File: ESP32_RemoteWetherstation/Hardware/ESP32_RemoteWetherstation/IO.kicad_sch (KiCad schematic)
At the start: 0 parts

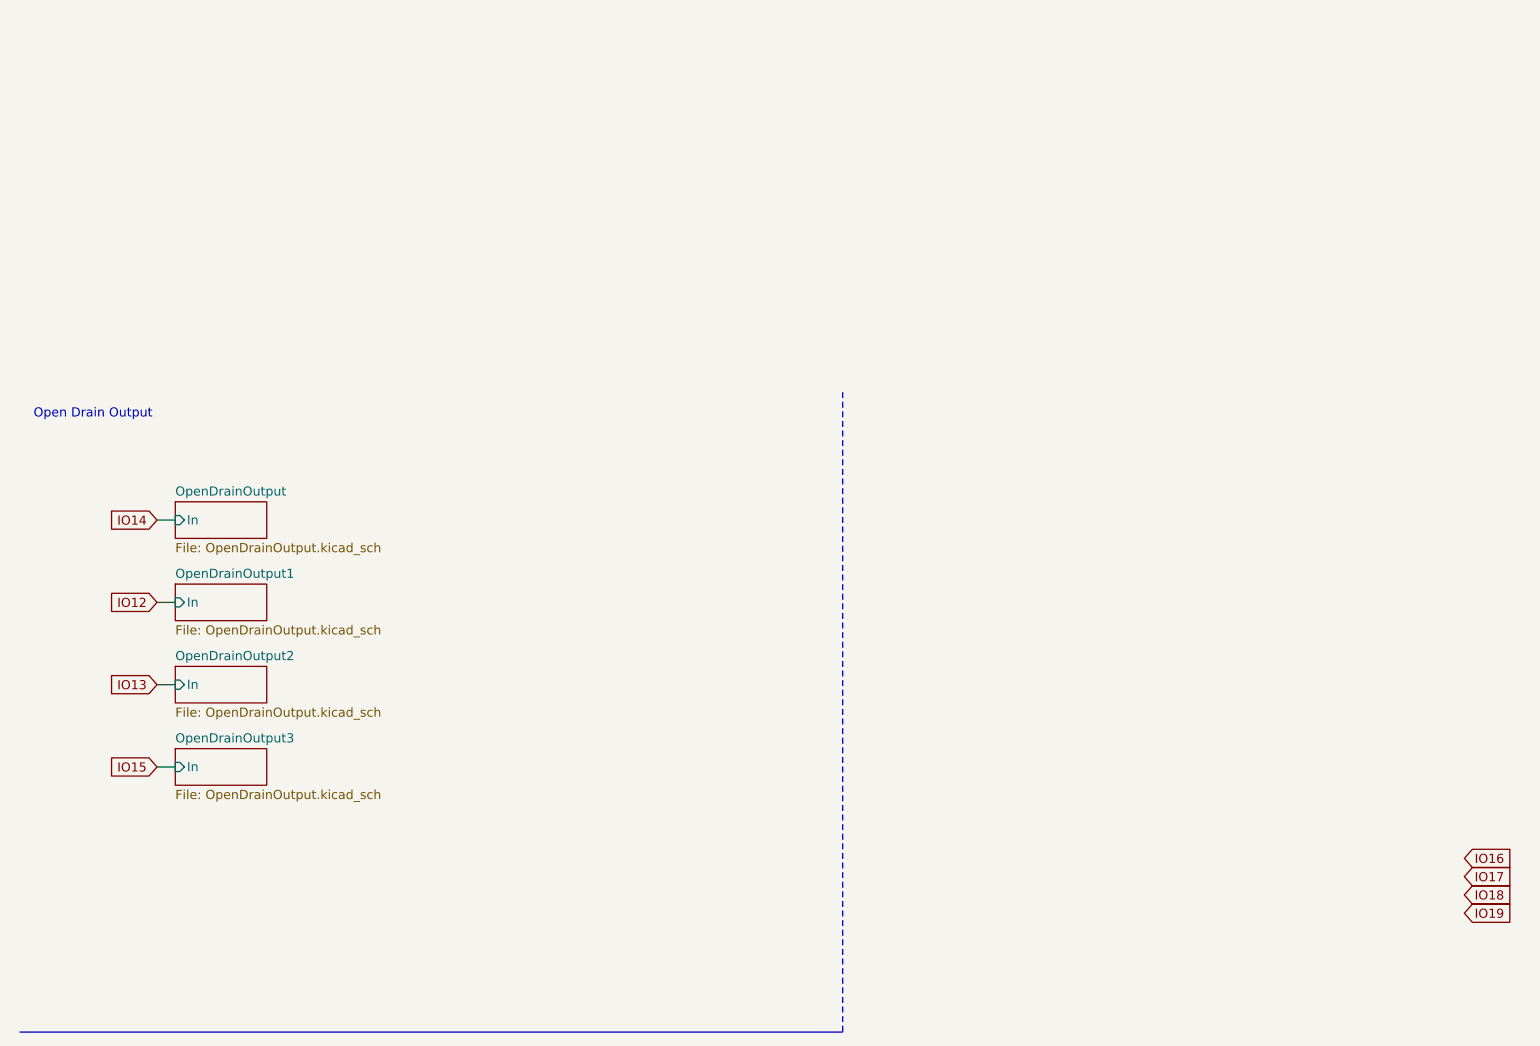
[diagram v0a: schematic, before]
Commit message: added Inputs
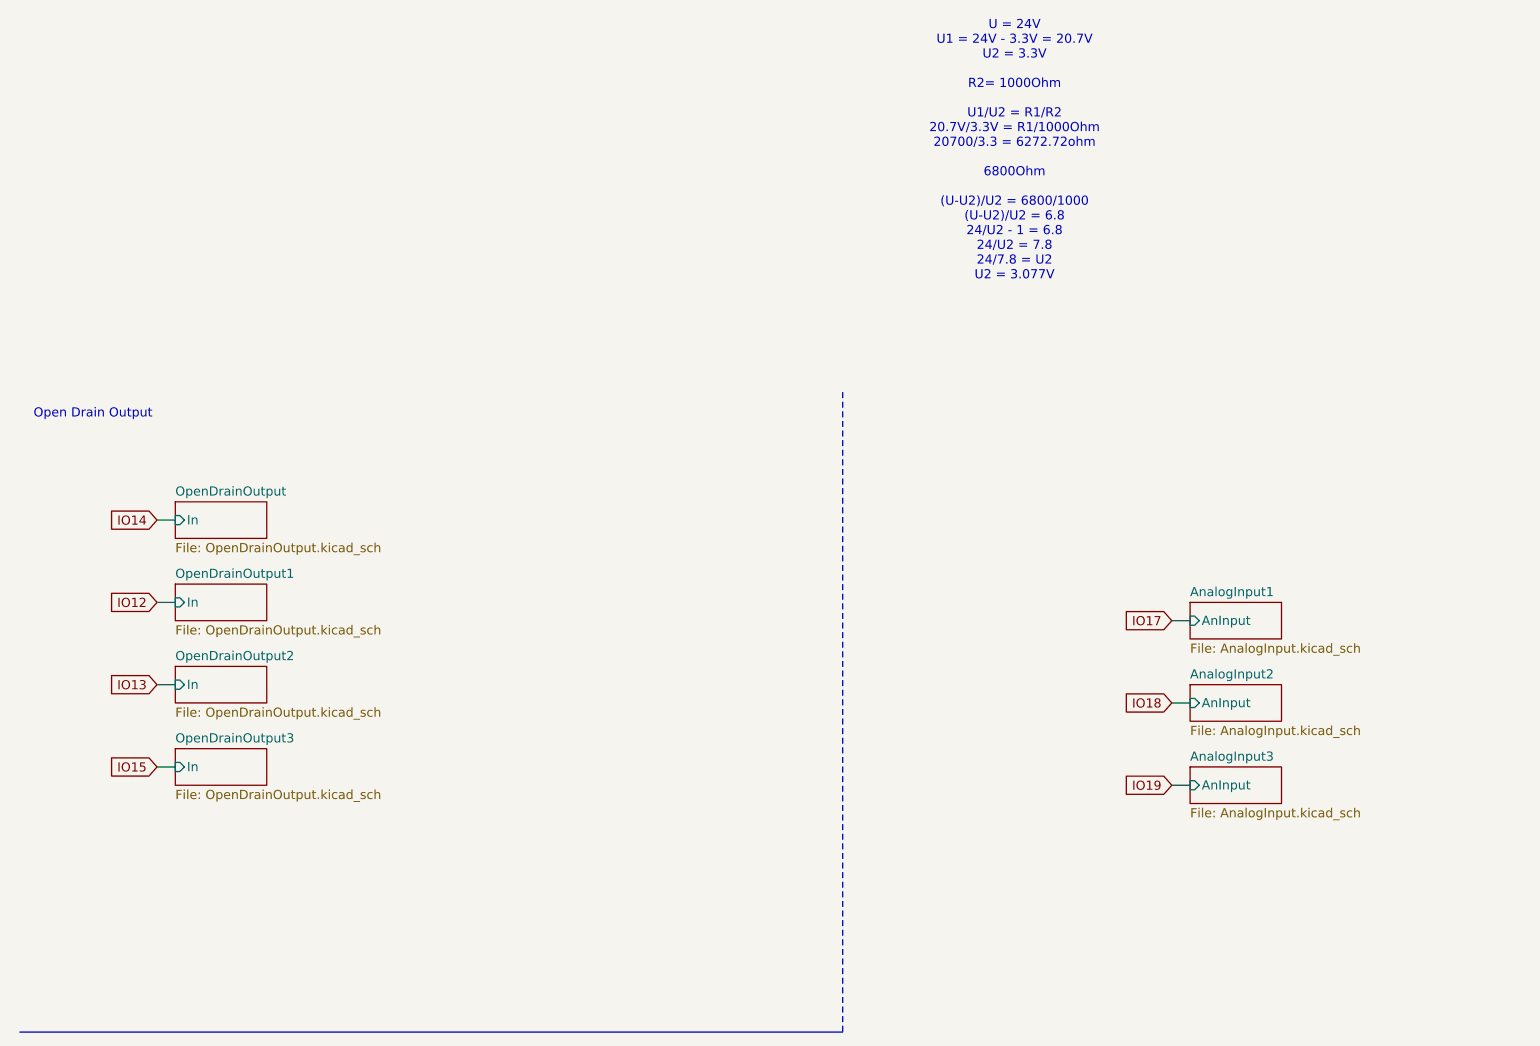
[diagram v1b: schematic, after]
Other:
- added sheet AnalogInput1 (AnalogInput.kicad_sch)
- added sheet AnalogInput2 (AnalogInput.kicad_sch)
- added sheet AnalogInput3 (AnalogInput.kicad_sch)
- note added: "U = 24V U1 = 24V - 3.3V = 20.7V U2 = 3.3V R2= 1000Ohm U1/U2 = R1/R2 20.7V/3.3V = R1/1000Ohm 20700/3.3 = 6272.72ohm 6800Ohm (U-U2)/U2 = 6800/1000 (U-U2)/U2 = 6.8 24/U2 - 1 = 6.8 24/U2 = 7.8 24/7.8 = U2 U2 = 3.077V"
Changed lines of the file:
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@@
+		)
+	)
+	(text "U = 24V\nU1 = 24V - 3.3V = 20.7V\nU2 = 3.3V\n\nR2= 1000Ohm\n\nU1/U2 = R1/R2\n20.7V/3.3V = R1/1000Ohm\n20700/3.3 = 6272.72ohm\n\n6800Ohm\n\n(U-U2)/U2 = 6800/1000\n(U-U2)/U2 = 6.8\n24/U2 - 1 = 6.8\n24/U2 = 7.8\n24/7.8 = U2\nU2 = 3.077V"
+		(exclude_from_sim no)
+		(at 150.876 -20.828 0)
+		(effects
+			(font
+				(size 1.27 1.27)
+			)
 		)
 	)
@@
 	(wire
 		(pts
+			(xy 172.72 67.31) (xy 175.26 67.31)
+		)
+		(stroke
+			(width 0)
+			(type default)
+		)
+	)
+	(wire
+		(pts
 			(xy 31.75 30.48) (xy 34.29 30.48)
 		)
@@
 		)
 	)
+	(wire
+		(pts
+			(xy 172.72 44.45) (xy 175.26 44.45)
+		)
+		(stroke
+			(width 0)
+			(type default)
+		)
+	)
+	(wire
+		(pts
+			(xy 172.72 55.88) (xy 175.26 55.88)
+		)
+		(stroke
+			(width 0)
+			(type default)
+		)
+	)
 	(global_label "IO14"
 		(shape input)
@@
 	(global_label "IO18"
 		(shape input)
-		(at 213.36 82.55 0)
-		(fields_autoplaced yes)
-		(effects
-			(font
-				(size 1.27 1.27)
-			)
-			(justify left)
-		)
-		(property "Intersheetrefs" "${INTERSHEET_REFS}"
-			(at 220.6995 82.55 0)
-			(effects
-				(font
-					(size 1.27 1.27)
-				)
-				(justify left)
+		(at 172.72 55.88 180)
+		(fields_autoplaced yes)
+		(effects
+			(font
+				(size 1.27 1.27)
+			)
+			(justify right)
+		)
+		(property "Intersheetrefs" "${INTERSHEET_REFS}"
+			(at 165.3805 55.88 0)
+			(effects
+				(font
+					(size 1.27 1.27)
+				)
+				(justify right)
 				(hide yes)
 			)
@@
 		)
 	)
-	(global_label "IO16"
-		(shape input)
-		(at 213.36 77.47 0)
-		(fields_autoplaced yes)
-		(effects
-			(font
-				(size 1.27 1.27)
-			)
-			(justify left)
-		)
-		(property "Intersheetrefs" "${INTERSHEET_REFS}"
-			(at 220.6995 77.47 0)
-			(effects
-				(font
-					(size 1.27 1.27)
-				)
-				(justify left)
-				(hide yes)
-			)
-		)
-	)
 	(global_label "IO19"
 		(shape input)
-		(at 213.36 85.09 0)
-		(fields_autoplaced yes)
-		(effects
-			(font
-				(size 1.27 1.27)
-			)
-			(justify left)
-		)
-		(property "Intersheetrefs" "${INTERSHEET_REFS}"
-			(at 220.6995 85.09 0)
-			(effects
-				(font
-					(size 1.27 1.27)
-				)
-				(justify left)
+		(at 172.72 67.31 180)
+		(fields_autoplaced yes)
+		(effects
+			(font
+				(size 1.27 1.27)
+			)
+			(justify right)
+		)
+		(property "Intersheetrefs" "${INTERSHEET_REFS}"
+			(at 165.3805 67.31 0)
+			(effects
+				(font
+					(size 1.27 1.27)
+				)
+				(justify right)
 				(hide yes)
 			)
@@
 	(global_label "IO17"
 		(shape input)
-		(at 213.36 80.01 0)
-		(fields_autoplaced yes)
-		(effects
-			(font
-				(size 1.27 1.27)
-			)
-			(justify left)
-		)
-		(property "Intersheetrefs" "${INTERSHEET_REFS}"
-			(at 220.6995 80.01 0)
-			(effects
-				(font
-					(size 1.27 1.27)
-				)
-				(justify left)
+		(at 172.72 44.45 180)
+		(fields_autoplaced yes)
+		(effects
+			(font
+				(size 1.27 1.27)
+			)
+			(justify right)
+		)
+		(property "Intersheetrefs" "${INTERSHEET_REFS}"
+			(at 165.3805 44.45 0)
+			(effects
+				(font
+					(size 1.27 1.27)
+				)
+				(justify right)
 				(hide yes)
 			)
@@
 	)
 	(sheet
+		(at 175.26 64.77)
+		(size 12.7 5.08)
+		(exclude_from_sim no)
+		(in_bom yes)
+		(on_board yes)
+		(dnp no)
+		(fields_autoplaced yes)
+		(stroke
+			(width 0.1524)
+			(type solid)
+		)
+		(fill
+			(color 0 0 0 0.0000)
+		)
+		(property "Sheetname" "AnalogInput3"
+			(at 175.26 64.0584 0)
+			(effects
+				(font
+					(size 1.27 1.27)
+				)
+				(justify left bottom)
+			)
+		)
+		(property "Sheetfile" "AnalogInput.kicad_sch"
+			(at 175.26 70.4346 0)
+			(effects
+				(font
+					(size 1.27 1.27)
+				)
+				(justify left top)
+			)
+		)
+		(pin "AnInput" input
+			(at 175.26 67.31 180)
+			(effects
+				(font
+					(size 1.27 1.27)
+				)
+				(justify left)
+			)
+		)
+		(instances
+			(project "ESP32_RemoteWetherstation"
+				(path "/bb194ab9-ddae-46dd-ae5d-1e0c862ad374/4641ced3-b603-4979-9d30-21d259fc76b1"
+					(page "11")
+				)
+			)
+		)
+	)
+	(sheet
 		(at 34.29 39.37)
 		(size 12.7 5.08)
@@
 	)
 	(sheet
+		(at 175.26 41.91)
+		(size 12.7 5.08)
+		(exclude_from_sim no)
+		(in_bom yes)
+		(on_board yes)
+		(dnp no)
+		(fields_autoplaced yes)
+		(stroke
+			(width 0.1524)
+			(type solid)
+		)
+		(fill
+			(color 0 0 0 0.0000)
+		)
+		(property "Sheetname" "AnalogInput1"
+			(at 175.26 41.1984 0)
+			(effects
+				(font
+					(size 1.27 1.27)
+				)
+				(justify left bottom)
+			)
+		)
+		(property "Sheetfile" "AnalogInput.kicad_sch"
+			(at 175.26 47.5746 0)
+			(effects
+				(font
+					(size 1.27 1.27)
+				)
+				(justify left top)
+			)
+		)
+		(pin "AnInput" input
+			(at 175.26 44.45 180)
+			(effects
+				(font
+					(size 1.27 1.27)
+				)
+				(justify left)
+			)
+		)
+		(instances
+			(project "ESP32_RemoteWetherstation"
+				(path "/bb194ab9-ddae-46dd-ae5d-1e0c862ad374/4641ced3-b603-4979-9d30-21d259fc76b1"
+					(page "8")
+				)
+			)
+		)
+	)
+	(sheet
 		(at 34.29 27.94)
 		(size 12.7 5.08)
@@
 				)
 			)
+		)
+	)
+	(sheet
+		(at 175.26 53.34)
+		(size 12.7 5.08)
+		(exclude_from_sim no)
+		(in_bom yes)
+		(on_board yes)
+		(dnp no)
+		(fields_autoplaced yes)
+		(stroke
+			(width 0.1524)
+			(type solid)
+		)
+		(fill
+			(color 0 0 0 0.0000)
+		)
+		(property "Sheetname" "AnalogInput2"
+			(at 175.26 52.6284 0)
+			(effects
+				(font
+					(size 1.27 1.27)
+				)
+				(justify left bottom)
+			)
+		)
+		(property "Sheetfile" "AnalogInput.kicad_sch"
+			(at 175.26 59.0046 0)
+			(effects
+				(font
+					(size 1.27 1.27)
+				)
+				(justify left top)
+			)
+		)
+		(pin "AnInput" input
+			(at 175.26 55.88 180)
+			(effects
+				(font
+					(size 1.27 1.27)
+				)
+				(justify left)
+			)
+		)
+		(instances
+			(project "ESP32_RemoteWetherstation"
+				(path "/bb194ab9-ddae-46dd-ae5d-1e0c862ad374/4641ced3-b603-4979-9d30-21d259fc76b1"
+					(page "10")
+				)
+			)

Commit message: edited schematic looks
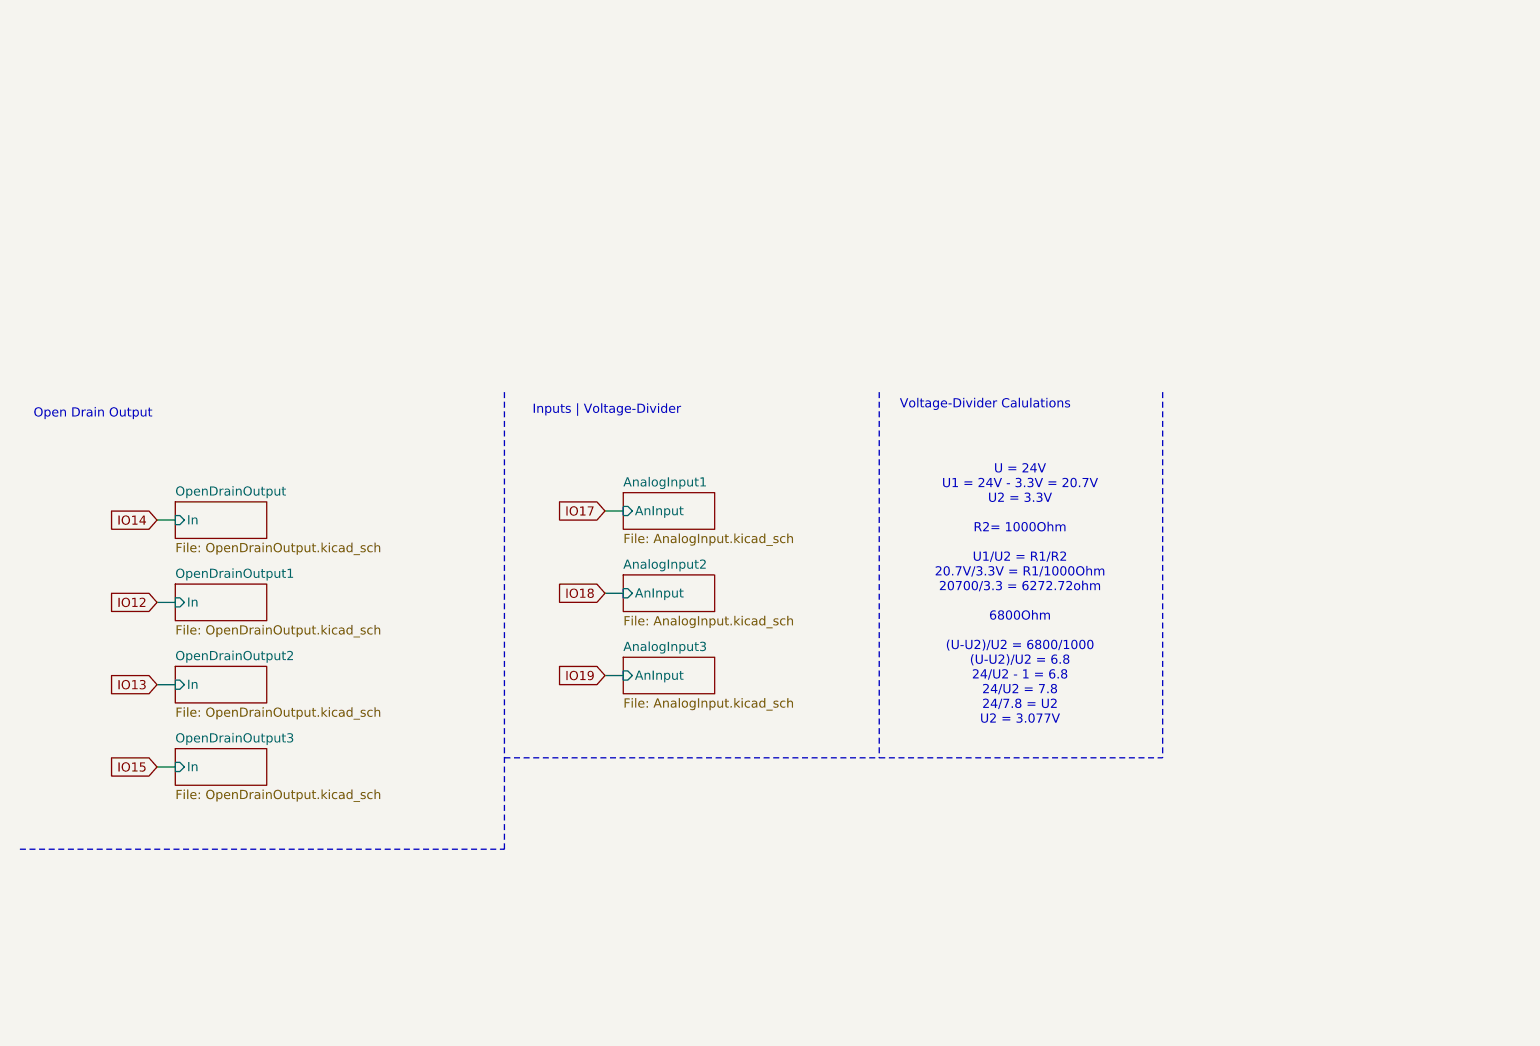
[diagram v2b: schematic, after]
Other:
- note added: "Inputs | Voltage-Divider"
- note added: "Voltage-Divider Calulations"
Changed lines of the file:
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@@
 	(generator_version "9.0")
 	(paper "A4")
+	(text "Voltage-Divider Calulations"
+		(exclude_from_sim no)
+		(at 146.812 14.478 0)
+		(effects
+			(font
+				(size 1.27 1.27)
+			)
+		)
+	)
 	(text "Open Drain Output"
 		(exclude_from_sim no)
@@
 	(text "U = 24V\nU1 = 24V - 3.3V = 20.7V\nU2 = 3.3V\n\nR2= 1000Ohm\n\nU1/U2 = R1/R2\n20.7V/3.3V = R1/1000Ohm\n20700/3.3 = 6272.72ohm\n\n6800Ohm\n\n(U-U2)/U2 = 6800/1000\n(U-U2)/U2 = 6.8\n24/U2 - 1 = 6.8\n24/U2 = 7.8\n24/7.8 = U2\nU2 = 3.077V"
 		(exclude_from_sim no)
-		(at 150.876 -20.828 0)
+		(at 151.638 40.894 0)
+		(effects
+			(font
+				(size 1.27 1.27)
+			)
+		)
+	)
+	(text "Inputs | Voltage-Divider"
+		(exclude_from_sim no)
+		(at 94.234 15.24 0)
 		(effects
 			(font
@@
 	(polyline
 		(pts
-			(xy 12.7 101.6) (xy 127 101.6)
+			(xy 171.45 12.7) (xy 171.45 63.5)
+		)
+		(stroke
+			(width 0)
+			(type dash)
+		)
+	)
+	(wire
+		(pts
+			(xy 93.98 52.07) (xy 96.52 52.07)
 		)
 		(stroke
@@
 	(wire
 		(pts
-			(xy 172.72 67.31) (xy 175.26 67.31)
+			(xy 31.75 30.48) (xy 34.29 30.48)
 		)
 		(stroke
@@
 	(wire
 		(pts
-			(xy 31.75 30.48) (xy 34.29 30.48)
+			(xy 31.75 64.77) (xy 34.29 64.77)
 		)
 		(stroke
@@
 		)
 	)
+	(polyline
+		(pts
+			(xy 80.01 12.7) (xy 80.01 76.2)
+		)
+		(stroke
+			(width 0)
+			(type dash)
+		)
+	)
+	(polyline
+		(pts
+			(xy 80.01 63.5) (xy 132.08 63.5)
+		)
+		(stroke
+			(width 0)
+			(type dash)
+		)
+	)
 	(wire
 		(pts
-			(xy 31.75 64.77) (xy 34.29 64.77)
+			(xy 93.98 29.21) (xy 96.52 29.21)
 		)
 		(stroke
@@
 		)
 	)
+	(wire
+		(pts
+			(xy 93.98 40.64) (xy 96.52 40.64)
+		)
+		(stroke
+			(width 0)
+			(type default)
+		)
+	)
 	(polyline
 		(pts
-			(xy 127 12.7) (xy 127 101.6)
+			(xy 132.08 12.7) (xy 132.08 63.5)
 		)
 		(stroke
@@
 		)
 	)
-	(wire
-		(pts
-			(xy 172.72 44.45) (xy 175.26 44.45)
-		)
-		(stroke
-			(width 0)
-			(type default)
-		)
-	)
-	(wire
-		(pts
-			(xy 172.72 55.88) (xy 175.26 55.88)
-		)
-		(stroke
-			(width 0)
-			(type default)
+	(polyline
+		(pts
+			(xy 132.08 63.5) (xy 171.45 63.5)
+		)
+		(stroke
+			(width 0)
+			(type dash)
+		)
+	)
+	(polyline
+		(pts
+			(xy 12.7 76.2) (xy 80.01 76.2)
+		)
+		(stroke
+			(width 0)
+			(type dash)
 		)
 	)
@@
 	(global_label "IO18"
 		(shape input)
-		(at 172.72 55.88 180)
+		(at 93.98 40.64 180)
 		(fields_autoplaced yes)
 		(effects
@@
 		)
 		(property "Intersheetrefs" "${INTERSHEET_REFS}"
-			(at 165.3805 55.88 0)
+			(at 86.6405 40.64 0)
 			(effects
 				(font
@@
 	(global_label "IO19"
 		(shape input)
-		(at 172.72 67.31 180)
+		(at 93.98 52.07 180)
 		(fields_autoplaced yes)
 		(effects
@@
 		)
 		(property "Intersheetrefs" "${INTERSHEET_REFS}"
-			(at 165.3805 67.31 0)
+			(at 86.6405 52.07 0)
 			(effects
 				(font
@@
 	(global_label "IO17"
 		(shape input)
-		(at 172.72 44.45 180)
+		(at 93.98 29.21 180)
 		(fields_autoplaced yes)
 		(effects
@@
 		)
 		(property "Intersheetrefs" "${INTERSHEET_REFS}"
-			(at 165.3805 44.45 0)
+			(at 86.6405 29.21 0)
 			(effects
 				(font
@@
 	)
 	(sheet
-		(at 175.26 64.77)
+		(at 96.52 49.53)
 		(size 12.7 5.08)
 		(exclude_from_sim no)
@@
 		)
 		(property "Sheetname" "AnalogInput3"
-			(at 175.26 64.0584 0)
+			(at 96.52 48.8184 0)
 			(effects
 				(font
@@
 		)
 		(property "Sheetfile" "AnalogInput.kicad_sch"
-			(at 175.26 70.4346 0)
+			(at 96.52 55.1946 0)
 			(effects
 				(font
@@
 		)
 		(pin "AnInput" input
-			(at 175.26 67.31 180)
+			(at 96.52 52.07 180)
 			(effects
 				(font
@@
 	)
 	(sheet
-		(at 175.26 41.91)
+		(at 96.52 26.67)
 		(size 12.7 5.08)
 		(exclude_from_sim no)
@@
 		)
 		(property "Sheetname" "AnalogInput1"
-			(at 175.26 41.1984 0)
+			(at 96.52 25.9584 0)
 			(effects
 				(font
@@
 		)
 		(property "Sheetfile" "AnalogInput.kicad_sch"
-			(at 175.26 47.5746 0)
+			(at 96.52 32.3346 0)
 			(effects
 				(font
@@
 		)
 		(pin "AnInput" input
-			(at 175.26 44.45 180)
+			(at 96.52 29.21 180)
 			(effects
 				(font
@@
 	)
 	(sheet
-		(at 175.26 53.34)
+		(at 96.52 38.1)
 		(size 12.7 5.08)
 		(exclude_from_sim no)
@@
 		)
 		(property "Sheetname" "AnalogInput2"
-			(at 175.26 52.6284 0)
+			(at 96.52 37.3884 0)
 			(effects
 				(font
@@
 		)
 		(property "Sheetfile" "AnalogInput.kicad_sch"
-			(at 175.26 59.0046 0)
+			(at 96.52 43.7646 0)
 			(effects
 				(font
@@
 		)
 		(pin "AnInput" input
-			(at 175.26 55.88 180)
-			(effects
-				(font
+			(at 96.52 40.64 180)
+			(effects
+				(font

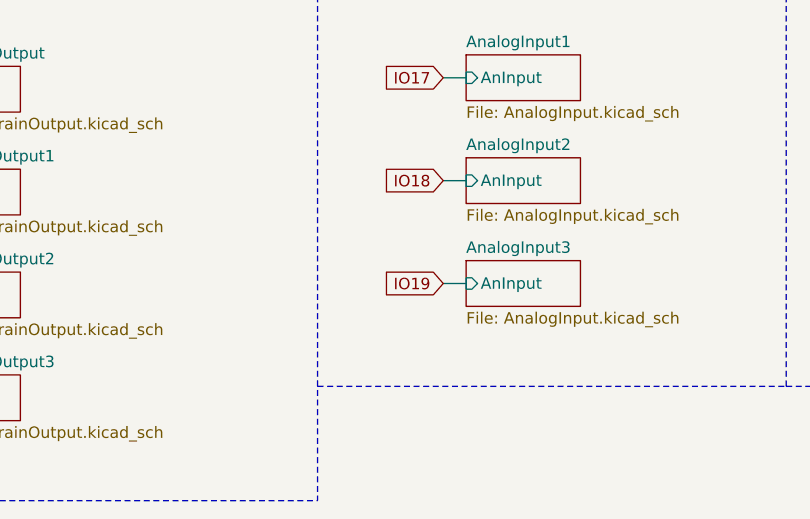
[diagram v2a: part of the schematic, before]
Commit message: changed MCU
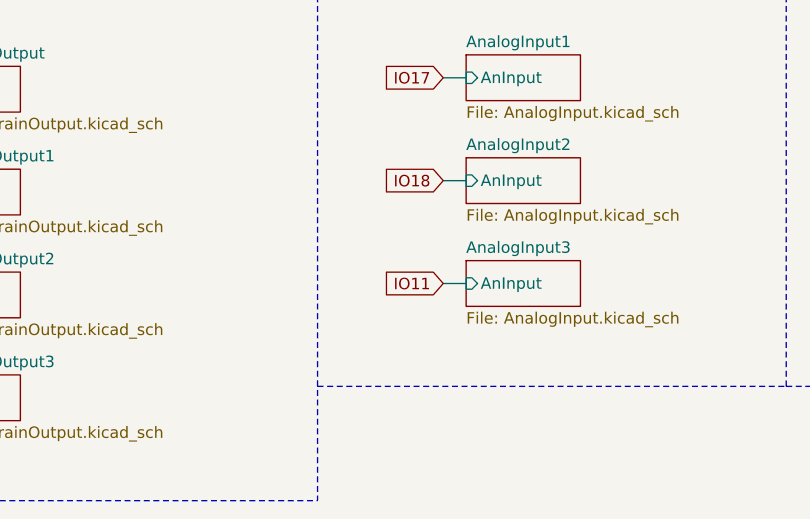
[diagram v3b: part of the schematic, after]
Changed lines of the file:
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@@
 		)
 	)
-	(global_label "IO19"
+	(global_label "IO11"
 		(shape input)
 		(at 93.98 52.07 180)
